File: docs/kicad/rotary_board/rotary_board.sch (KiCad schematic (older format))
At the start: 8 parts, among them J1 Conn_01x05, SW1 ROT1, SW2 ROT2, SW3 ROT3, SW4 ROT4, U1 mcp23017

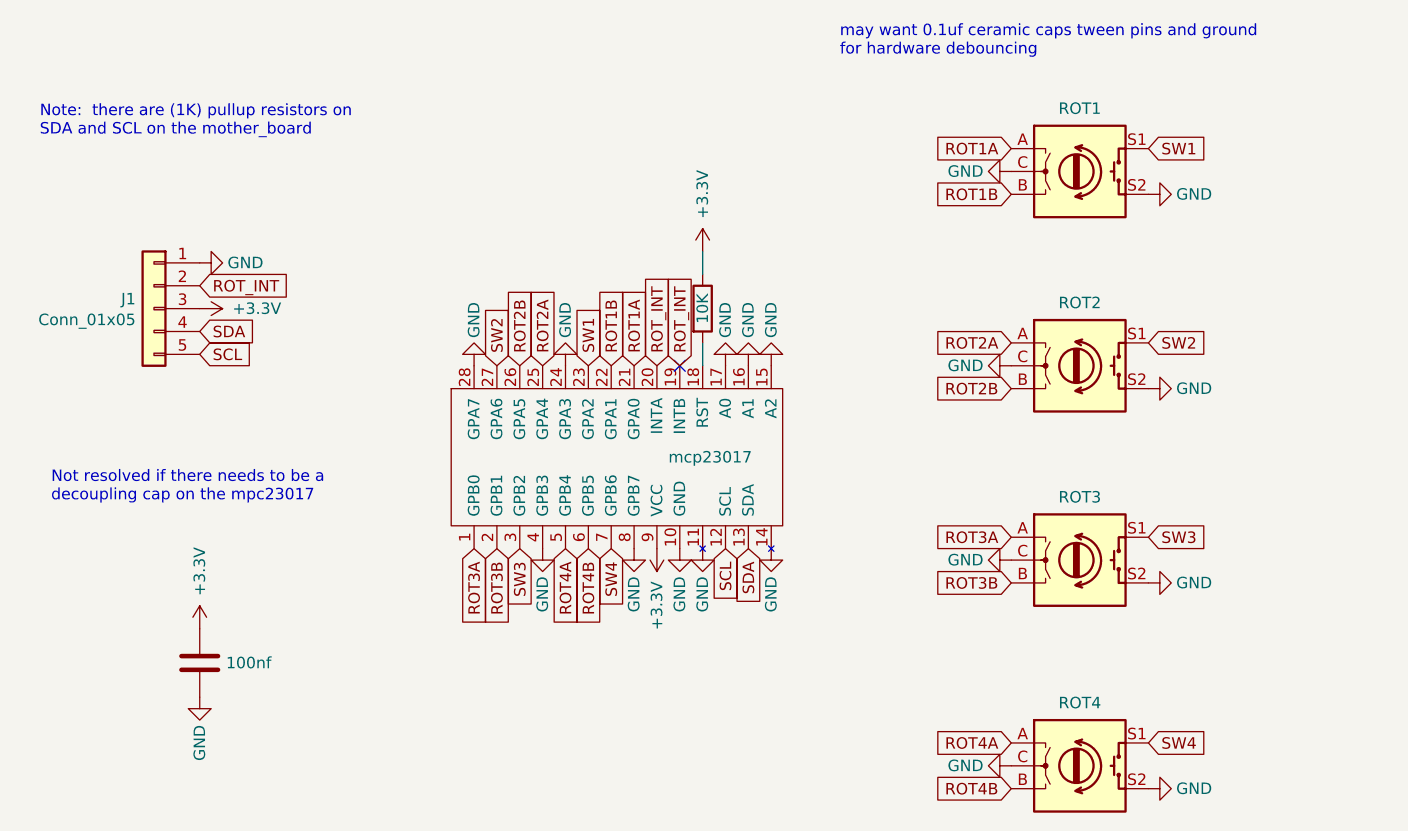
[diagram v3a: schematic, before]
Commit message: final initial TE3 PCBS - updated LED board green resistor to 1K - changed TE3 display SCLK to pin13 as it is required for hardware SPI0 - changed nomenclature of rotary board to ROT0..ROT4 and corrected order to match named rotary 1..4
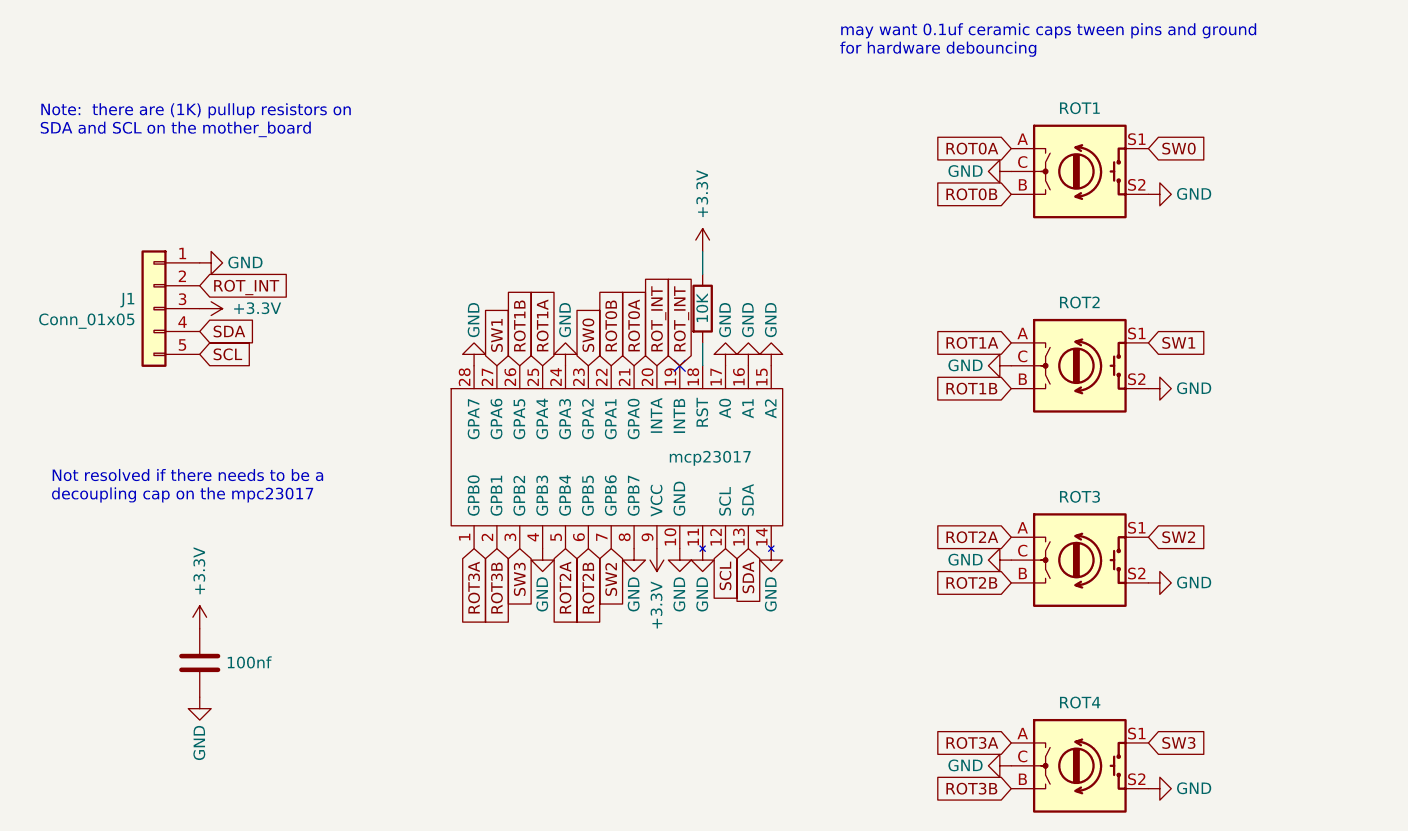
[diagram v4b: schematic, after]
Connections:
- net ROT1A: now also SW2.A, U1.25 (GPA4); no longer SW1.A, U1.21 (GPA0)
- net ROT1B: now also SW2.B, U1.26 (GPA5); no longer SW1.B, U1.22 (GPA1)
- net ROT2A: now also SW3.A, U1.5 (GPB4); no longer SW2.A, U1.25 (GPA4)
- net ROT2B: now also SW3.B, U1.6 (GPB5); no longer SW2.B, U1.26 (GPA5)
- net ROT3A: now also SW4.A; no longer SW3.A
- net ROT3B: now also SW4.B; no longer SW3.B
- net SW1: now also SW2.S1, U1.27 (GPA6); no longer SW1.S1, U1.23 (GPA2)
- net SW2: now also SW3.S1, U1.7 (GPB6); no longer SW2.S1, U1.27 (GPA6)
- net SW3: now also SW4.S1; no longer SW3.S1
- removed net ROT4A: SW4.A, U1.5 (GPB4)
- removed net ROT4B: SW4.B, U1.6 (GPB5)
- removed net SW4: SW4.S1, U1.7 (GPB6)
- new net ROT0A: SW1.A, U1.21 (GPA0)
- new net ROT0B: SW1.B, U1.22 (GPA1)
- new net SW0: SW1.S1, U1.23 (GPA2)
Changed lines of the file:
@@
-$EndComp
-$Comp
-L Device:Rotary_Encoder_Switch SW3
-U 1 1 663F4490
-P 6500 3150
-F 0 "SW3" H 6500 3517 50  0001 C CNN
-F 1 "ROT3" H 6500 3425 50  0000 C CNN
-F 2 "0_my_footprints:myRotaryEncoder" H 6350 3310 50  0001 C CNN
-F 3 "~" H 6500 3410 50  0001 C CNN
-	1    6500 3150
-	1    0    0    -1
-$EndComp
-$Comp
-L Device:Rotary_Encoder_Switch SW4
-U 1 1 663F4B46
-P 6500 4050
-F 0 "SW4" H 6500 4417 50  0001 C CNN
-F 1 "ROT4" H 6500 4325 50  0000 C CNN
-F 2 "0_my_footprints:myRotaryEncoder" H 6350 4210 50  0001 C CNN
-F 3 "~" H 6500 4310 50  0001 C CNN
-	1    6500 4050
-	1    0    0    -1
 $EndComp
 $Comp
@@
 $EndComp
 Text GLabel 6800 1350 2    50   Input ~ 0
-SW1
-Text GLabel 6800 2200 2    50   Input ~ 0
+SW0
+Text GLabel 6800 3050 2    50   Input ~ 0
 SW2
-Text GLabel 6800 3050 2    50   Input ~ 0
-SW3
-Text GLabel 6800 3950 2    50   Input ~ 0
-SW4
 Text GLabel 6200 1350 0    50   Input ~ 0
-ROT1A
+ROT0A
 Text GLabel 6200 1550 0    50   Input ~ 0
-ROT1B
-Text GLabel 6200 2200 0    50   Input ~ 0
+ROT0B
+Text GLabel 6200 3050 0    50   Input ~ 0
 ROT2A
-Text GLabel 6200 2400 0    50   Input ~ 0
+Text GLabel 6200 3250 0    50   Input ~ 0
 ROT2B
-Text GLabel 6200 3050 0    50   Input ~ 0
-ROT3A
-Text GLabel 6200 3250 0    50   Input ~ 0
-ROT3B
-Text GLabel 6200 3950 0    50   Input ~ 0
-ROT4A
-Text GLabel 6200 4150 0    50   Input ~ 0
-ROT4B
 $Comp
 L power:GND #PWR012
@@
 $EndComp
 $Comp
-L power:GND #PWR020
-U 1 1 66427662
-P 6800 3250
-F 0 "#PWR020" H 6800 3000 50  0001 C CNN
-F 1 "GND" V 6800 3050 50  0000 C CNN
-F 2 "" H 6800 3250 50  0001 C CNN
-F 3 "" H 6800 3250 50  0001 C CNN
-	1    6800 3250
-	0    -1   -1   0
-$EndComp
-$Comp
-L power:GND #PWR024
-U 1 1 66427948
-P 6800 4150
-F 0 "#PWR024" H 6800 3900 50  0001 C CNN
-F 1 "GND" V 6800 3950 50  0000 C CNN
-F 2 "" H 6800 4150 50  0001 C CNN
-F 3 "" H 6800 4150 50  0001 C CNN
-	1    6800 4150
-	0    -1   -1   0
-$EndComp
-$Comp
 L power:GND #PWR02
 U 1 1 66428D78
@@
 $EndComp
 $Comp
-L power:GND #PWR019
-U 1 1 6642A07A
-P 6200 3150
-F 0 "#PWR019" H 6200 2900 50  0001 C CNN
-F 1 "GND" V 6200 2950 50  0000 C CNN
-F 2 "" H 6200 3150 50  0001 C CNN
-F 3 "" H 6200 3150 50  0001 C CNN
-	1    6200 3150
-	0    1    1    0
-$EndComp
-$Comp
-L power:GND #PWR023
-U 1 1 6642A3A3
-P 6200 4050
-F 0 "#PWR023" H 6200 3800 50  0001 C CNN
-F 1 "GND" V 6200 3850 50  0000 C CNN
-F 2 "" H 6200 4050 50  0001 C CNN
-F 3 "" H 6200 4050 50  0001 C CNN
-	1    6200 4050
-	0    1    1    0
-$EndComp
-$Comp
 L power:+3.3V #PWR015
 U 1 1 6643C635
@@
 Wire Wire Line
 	4850 1800 4850 1900
-Text GLabel 4550 2300 1    50   Input ~ 0
-ROT1A
-Text GLabel 4450 2300 1    50   Input ~ 0
-ROT1B
-Text GLabel 4150 2300 1    50   Input ~ 0
-ROT2A
-Text GLabel 4050 2300 1    50   Input ~ 0
-ROT2B
 Text GLabel 3850 3100 3    50   Input ~ 0
 ROT3A
 Text GLabel 3950 3100 3    50   Input ~ 0
 ROT3B
-Text GLabel 4250 3100 3    50   Input ~ 0
-ROT4A
-Text GLabel 4350 3100 3    50   Input ~ 0
-ROT4B
-Text GLabel 4350 2300 1    50   Input ~ 0
-SW1
-Text GLabel 3950 2300 1    50   Input ~ 0
-SW2
 Text GLabel 4050 3100 3    50   Input ~ 0
 SW3
-Text GLabel 4450 3100 3    50   Input ~ 0
-SW4
 $Comp
 L 0_my_symbols:mcp23017 U1
@@
 	-1   0    0    1
 $EndComp
+$Comp
+L power:GND #PWR023
+U 1 1 6642A3A3
+P 6200 4050
+F 0 "#PWR023" H 6200 3800 50  0001 C CNN
+F 1 "GND" V 6200 3850 50  0000 C CNN
+F 2 "" H 6200 4050 50  0001 C CNN
+F 3 "" H 6200 4050 50  0001 C CNN
+	1    6200 4050
+	0    1    1    0
+$EndComp
+$Comp
+L power:GND #PWR024
+U 1 1 66427948
+P 6800 4150
+F 0 "#PWR024" H 6800 3900 50  0001 C CNN
+F 1 "GND" V 6800 3950 50  0000 C CNN
+F 2 "" H 6800 4150 50  0001 C CNN
+F 3 "" H 6800 4150 50  0001 C CNN
+	1    6800 4150
+	0    -1   -1   0
+$EndComp
+$Comp
+L Device:Rotary_Encoder_Switch SW4
+U 1 1 663F4B46
+P 6500 4050
+F 0 "SW4" H 6500 4417 50  0001 C CNN
+F 1 "ROT4" H 6500 4325 50  0000 C CNN
+F 2 "0_my_footprints:myRotaryEncoder" H 6350 4210 50  0001 C CNN
+F 3 "~" H 6500 4310 50  0001 C CNN
+	1    6500 4050
+	1    0    0    -1
+$EndComp
+$Comp
+L power:GND #PWR019
+U 1 1 6642A07A
+P 6200 3150
+F 0 "#PWR019" H 6200 2900 50  0001 C CNN
+F 1 "GND" V 6200 2950 50  0000 C CNN
+F 2 "" H 6200 3150 50  0001 C CNN
+F 3 "" H 6200 3150 50  0001 C CNN
+	1    6200 3150
+	0    1    1    0
+$EndComp
+$Comp
+L power:GND #PWR020
+U 1 1 66427662
+P 6800 3250
+F 0 "#PWR020" H 6800 3000 50  0001 C CNN
+F 1 "GND" V 6800 3050 50  0000 C CNN
+F 2 "" H 6800 3250 50  0001 C CNN
+F 3 "" H 6800 3250 50  0001 C CNN
+	1    6800 3250
+	0    -1   -1   0
+$EndComp
+Text GLabel 6200 4150 0    50   Input ~ 0
+ROT3B
+Text GLabel 6200 3950 0    50   Input ~ 0
+ROT3A
+Text GLabel 6800 3950 2    50   Input ~ 0
+SW3
+$Comp
+L Device:Rotary_Encoder_Switch SW3
+U 1 1 663F4490
+P 6500 3150
+F 0 "SW3" H 6500 3517 50  0001 C CNN
+F 1 "ROT3" H 6500 3425 50  0000 C CNN
+F 2 "0_my_footprints:myRotaryEncoder" H 6350 3310 50  0001 C CNN
+F 3 "~" H 6500 3410 50  0001 C CNN
+	1    6500 3150
+	1    0    0    -1
+$EndComp
+Text GLabel 4350 2300 1    50   Input ~ 0
+SW0
+Text GLabel 4450 2300 1    50   Input ~ 0
+ROT0B
+Text GLabel 4550 2300 1    50   Input ~ 0
+ROT0A
+Text GLabel 4350 3100 3    50   Input ~ 0
+ROT2B
+Text GLabel 4450 3100 3    50   Input ~ 0
+SW2
+Text GLabel 4250 3100 3    50   Input ~ 0
+ROT2A
+Text GLabel 3950 2300 1    50   Input ~ 0
+SW1
+Text GLabel 4050 2300 1    50   Input ~ 0
+ROT1B
+Text GLabel 4150 2300 1    50   Input ~ 0
+ROT1A
+Text GLabel 6200 2200 0    50   Input ~ 0
+ROT1A
+Text GLabel 6200 2400 0    50   Input ~ 0
+ROT1B
+Text GLabel 6800 2200 2    50   Input ~ 0
+SW1
 $EndSCHEMATC
